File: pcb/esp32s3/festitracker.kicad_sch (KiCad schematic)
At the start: 28 parts, among them Q1_Xtal1 32.0MHz, U1 SX1262IMLTRT, U2 PE4259

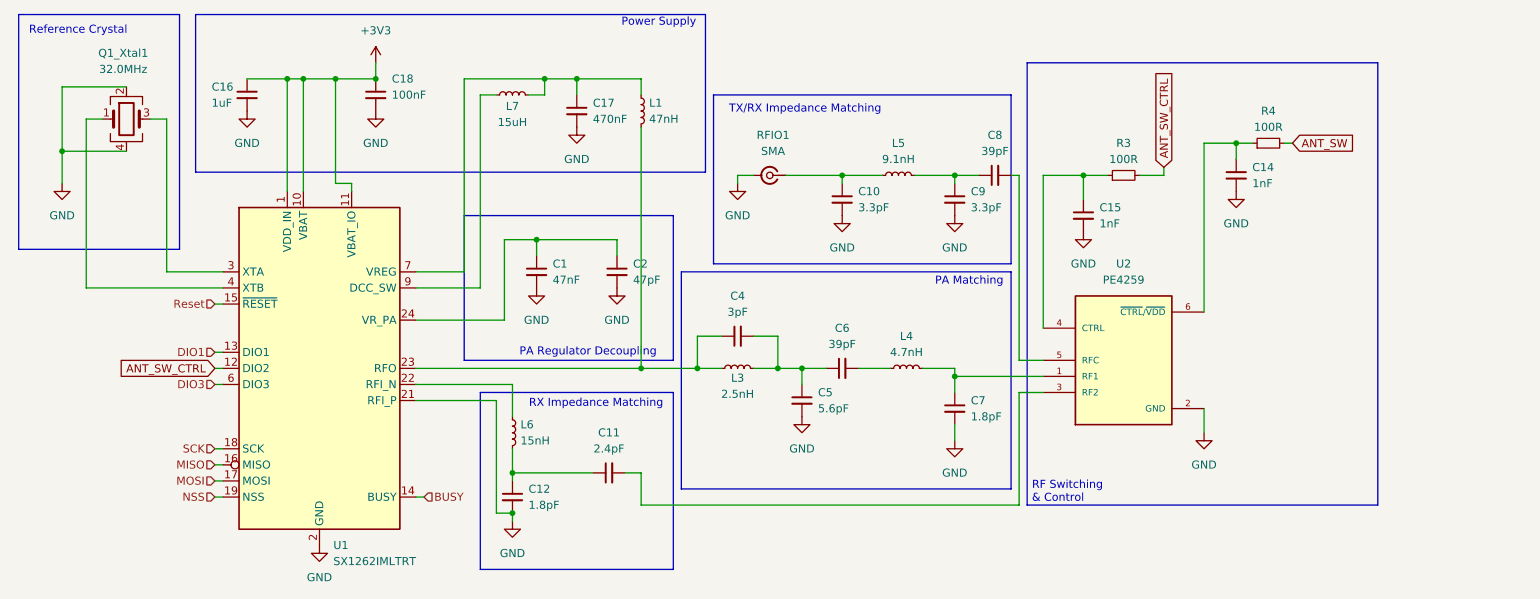
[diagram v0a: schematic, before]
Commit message: Update PCB with new components and footprints
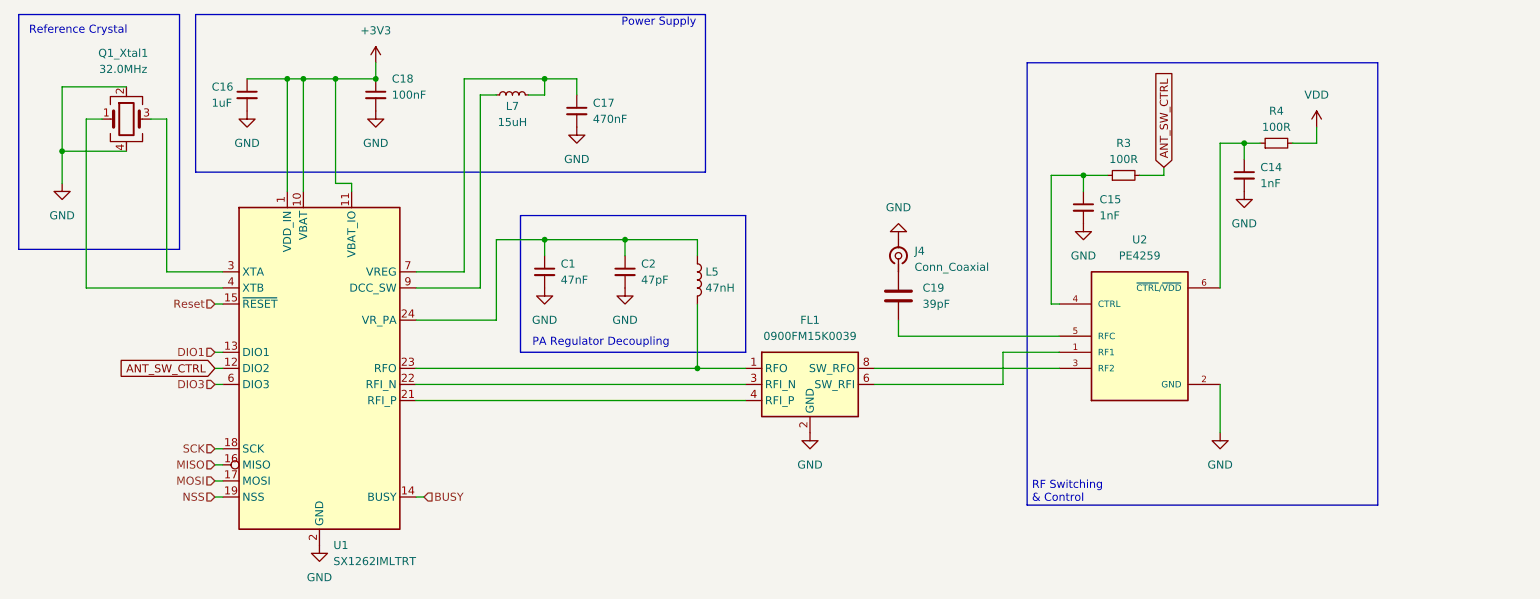
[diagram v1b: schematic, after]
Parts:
- removed C10, C9: 3.3pF, Capacitor_SMD:C_0402_1005Metric, symbol Device:C_Small
- removed C11: 2.4pF, Capacitor_SMD:C_0402_1005Metric, symbol Device:C_Small
- removed C12, C7: 1.8pF, Capacitor_SMD:C_0402_1005Metric, symbol Device:C_Small
- removed C4: 3pF, Capacitor_SMD:C_0402_1005Metric, symbol Device:C_Small
- removed C5: 5.6pF, Capacitor_SMD:C_0402_1005Metric, symbol Device:C_Small
- removed C6, C8: 39pF, Capacitor_SMD:C_0402_1005Metric, symbol Device:C_Small
- removed L1: 47nH, Inductor_SMD:L_0402_1005Metric, symbol Device:L_Small
- removed L3: 2.5nH, Inductor_SMD:L_0402_1005Metric, symbol Device:L_Small
- removed L4: 4.7nH, Inductor_SMD:L_0402_1005Metric, symbol Device:L_Small
- removed L5: 9.1nH, Inductor_SMD:L_0402_1005Metric, symbol Device:L_Small
- removed L6: 15nH, Inductor_SMD:L_0402_1005Metric, symbol Device:L_Small
- removed RFIO1: SMA, Connector_Coaxial:U.FL_Molex_MCRF_73412-0110_Vertical, symbol Connector:Conn_Coaxial_Small
- added C19: 39pF, Capacitor_SMD:C_0402_1005Metric, symbol Device:C
- added FL1: 0900FM15K0039, RF_Converter:Balun_Johanson_0900FM15K0039, symbol Filter:0900FM15K0039
- added J4: Conn_Coaxial, Connector_Coaxial:U.FL_Molex_MCRF_73412-0110_Vertical, symbol Connector:Conn_Coaxial_Small
- added L5: 47nH, Inductor_SMD:L_0402_1005Metric, symbol Device:L
- U2: footprint KiCAD Parts:SOT65P215X110-6N -> custom_comps:SOT65P215X110-6N
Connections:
- net GND: now also FL1.10 (GND), FL1.2 (GND), FL1.5 (GND), FL1.7 (GND), FL1.9 (GND), J4.2 (Ext); no longer U1.21 (RFI_P)
- net at U1.23 (RFO): now also FL1.1 (RFO), L5.2
- net at U1.22 (RFI_N): now also FL1.3 (RFI_N)
- net at U2.1 (RF1): now also FL1.6 (SW_RFI)
- net at C1.1, C2.1, U1.24 (VR_PA): now also L5.1
- net at U2.3 (RF2): now also FL1.8 (SW_RFO)
- net at U2.5 (RFC): now also C19.2
- net ANT_SW renamed VDD
- new net: FL1.4 (RFI_P), U1.21 (RFI_P)
- new net: C19.1, J4.1 (In)
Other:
- note removed: "PA Matching"
- note removed: "RX Impedance Matching"
- note removed: "TX/RX Impedance Matching"
- moved on the sheet: C1, C14, C15, C2, R4, U2

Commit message: pcb kinda almost done!
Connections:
- net VDD is gone; now on net +3V3: R4.2
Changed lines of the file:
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@@
-	)
-	(symbol
-		(lib_id "power:VDD")
-		(at 237.49 57.15 0)
-		(unit 1)
-		(exclude_from_sim no)
-		(in_bom yes)
-		(on_board yes)
-		(dnp no)
-		(fields_autoplaced yes)
-		(property "Reference" "#PWR053"
-			(at 237.49 60.96 0)
-			(effects
-				(font
-					(size 1.27 1.27)
-				)
-				(hide yes)
-			)
-		)
-		(property "Value" "VDD"
-			(at 237.49 52.07 0)
-			(effects
-				(font
-					(size 1.27 1.27)
-				)
-			)
-		)
-		(property "Footprint" ""
-			(at 237.49 57.15 0)
-			(effects
-				(font
-					(size 1.27 1.27)
-				)
-				(hide yes)
-			)
-		)
-		(property "Datasheet" ""
-			(at 237.49 57.15 0)
-			(effects
-				(font
-					(size 1.27 1.27)
-				)
-				(hide yes)
-			)
-		)
-		(property "Description" "Power symbol creates a global label with name \"VDD\""
-			(at 237.49 57.15 0)
-			(effects
-				(font
-					(size 1.27 1.27)
-				)
-				(hide yes)
-			)
-		)
-		(pin "1"
-		)
-		(instances
-			(project "esp32s3"
-				(path "/834edf73-57a5-43b4-ab36-0b077e93e6d5/47c9428f-e312-4c3e-af55-9dc14b1a0249"
-					(reference "#PWR053")
-					(unit 1)
-				)
-			)
-		)
 	)
 	(symbol
@@
 					(unit 1)
 				)
+			)
+		)
+	)
+	(symbol
+		(lib_id "power:+3V3")
+		(at 237.49 57.15 0)
+		(unit 1)
+		(exclude_from_sim no)
+		(in_bom yes)
+		(on_board yes)
+		(dnp no)
+		(fields_autoplaced yes)
+		(property "Reference" "#PWR053"
+			(at 237.49 60.96 0)
+			(effects
+				(font
+					(size 1.27 1.27)
+				)
+				(hide yes)
+			)
+		)
+		(property "Value" "+3V3"
+			(at 237.49 52.07 0)
+			(effects
+				(font
+					(size 1.27 1.27)
+				)
+			)
+		)
+		(property "Footprint" ""
+			(at 237.49 57.15 0)
+			(effects
+				(font
+					(size 1.27 1.27)
+				)
+				(hide yes)
+			)
+		)
+		(property "Datasheet" ""
+			(at 237.49 57.15 0)
+			(effects
+				(font
+					(size 1.27 1.27)
+				)
+				(hide yes)
+			)
+		)
+		(property "Description" "Power symbol creates a global label with name \"+3V3\""
+			(at 237.49 57.15 0)
+			(effects
+				(font
+					(size 1.27 1.27)
+				)
+				(hide yes)
+			)
+		)
+		(pin "1"
+		)
+		(instances
+			(project "esp32s3"
+				(path "/834edf73-57a5-43b4-ab36-0b077e93e6d5/47c9428f-e312-4c3e-af55-9dc14b1a0249"
+					(reference "#PWR053")
+					(unit 1)
+				)

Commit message: LORA
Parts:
- removed U2: PE4259, custom_comps:SOT65P215X110-6N, symbol PE4259:PE4259
- added U12: BGS12SN6E6327XTSA1, BGS12SN6:TSNP-6-2&slash_-8_INF, symbol BGS12SN6:BGS12SN6E6327XTSA1
- L7: footprint Inductor_SMD:L_0402_1005Metric -> Inductor_SMD:L_0805_2012Metric
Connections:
- net GND: now also U12.2 (GND)
- net at C14.1, R4.1: now also U12.4 (VDD)
- net at C15.1, R3.1: now also U12.6 (CTRL)
- net at C19.2: now also U12.5 (RFIN)
- net at FL1.6 (SW_RFI): now also U12.3 (RF1)
- net at FL1.8 (SW_RFO): now also U12.1 (RF2)
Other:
- moved on the sheet: C14, C15, R3, R4
